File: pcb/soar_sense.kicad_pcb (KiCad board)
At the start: 4 copper layers, 42.7 x 23.1 mm, 55 parts, among them J1 Conn_02x03_Top_Bottom, J3 Conn_02x02_Top_Bottom, J4 Conn_02x02_Top_Bottom, J5 Conn_02x02_Top_Bottom, J6 Conn_02x03_Top_Bottom, J7 Conn_02x03_Top_Bottom, J8 Conn_01x06, U1 SPX3819M5-L-3-3, U2 STM32F103CBTx, U3 SHT35-DIS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

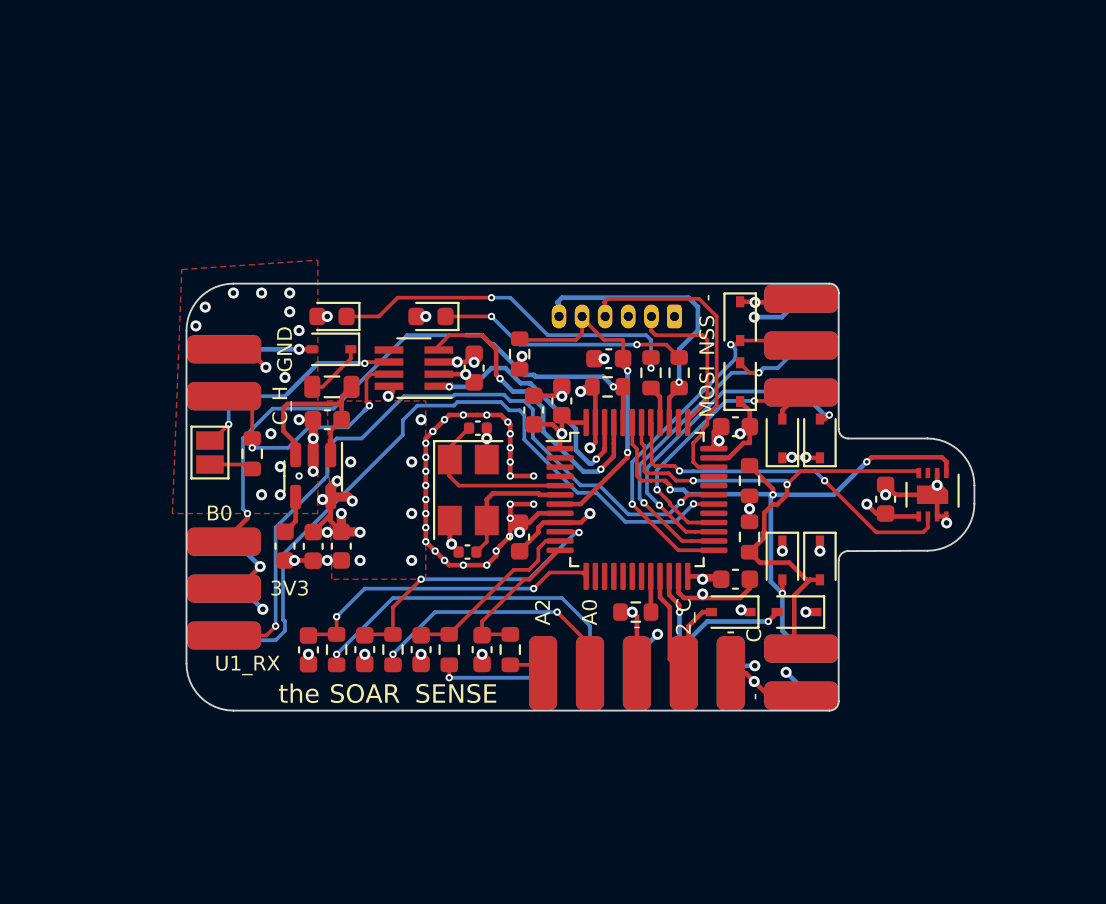
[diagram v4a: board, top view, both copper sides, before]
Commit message: added supply voltage sensing
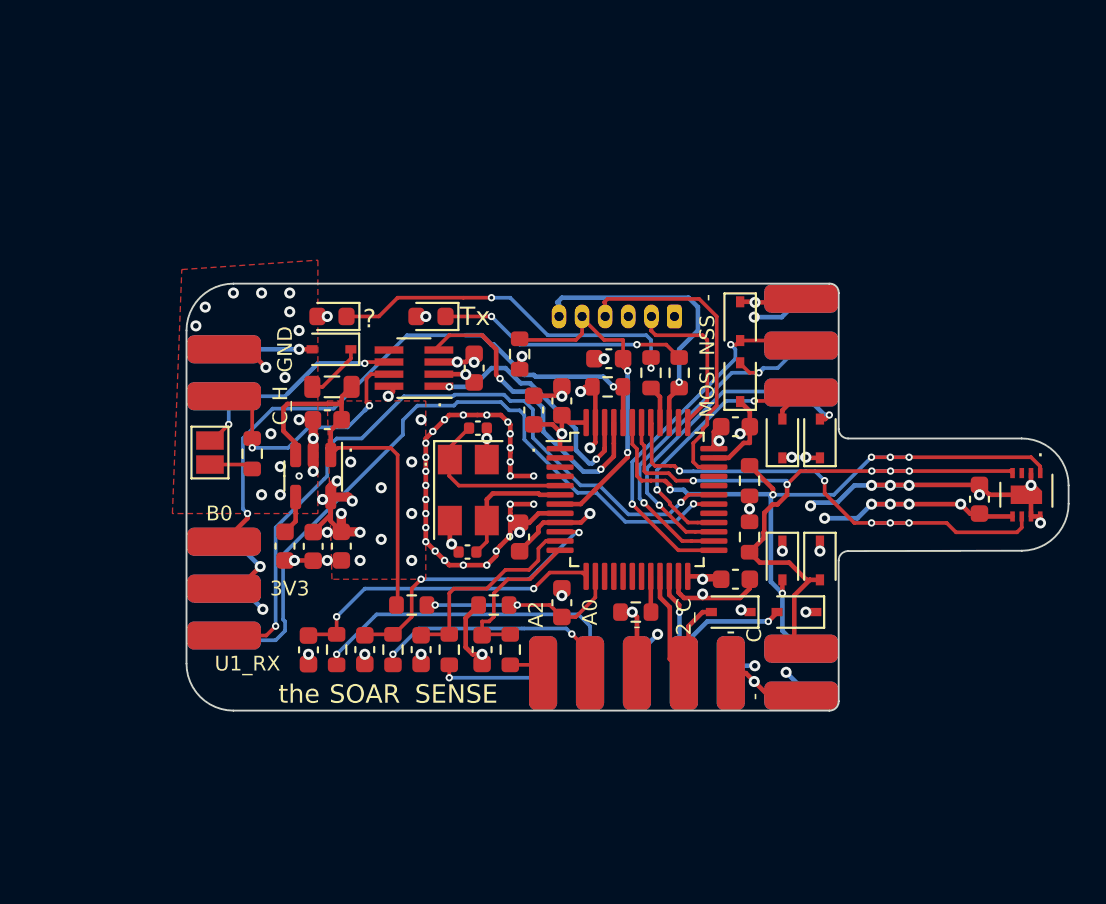
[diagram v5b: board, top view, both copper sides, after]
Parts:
- added C18: 100n, Capacitor_SMD:C_0603_1608Metric, F.Cu at (142.7, 110.7)
- added R3: 27k, Resistor_SMD:R_0603_1608Metric, F.Cu at (134.6, 110.9)
- added R4: 4k7, Resistor_SMD:R_0603_1608Metric, F.Cu at (139.1, 110.9)
- moved C13 5.08 mm to (165.4, 105.1)
- moved U3 5.08 mm to (167.9, 104.9)
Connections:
- U2 pad 14: unconnected-(U2-Pad14) -> ADC_IN4
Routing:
- net GND: track 91.5 -> 107.1 mm, vias 74 -> 79
- net Net-(C1-Pad1): track 10.3 -> 22.3 mm
- net ADC_IN4: track 0.00 -> 11.4 mm, vias 0 -> 2
- net +3V3: track 47.9 -> 57.6 mm, vias 28 -> 34
- net SHT_RST: track 19.4 -> 26.9 mm, vias 2 -> 5
- net I2C1_SCL: track 31.6 -> 38.7 mm, vias 2 -> 5
- net I2C1_SDA: track 33.8 -> 40.8 mm, vias 4 -> 6
- net ADC_IN1: track 10.0 -> 11.3 mm
- net ADC_IN2: track 8.11 -> 8.85 mm
- net ADC_INPUT3: track 18.7 -> 18.0 mm
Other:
- board size 42.7 x 23.1 mm -> 47.8 x 23.1 mm
- board text added: "."
- board text added: "12.4mm"
- board text added: "47.7mm"
- board text added: "?"
- board text added: "Tx"
- board text removed: "42.7mm"
- board text removed: "7.4mm"

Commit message: added holes
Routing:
- net GND: vias 79 -> 76
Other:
- outline, holes or cut-outs redrawn
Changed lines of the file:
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@@
     )
   )
+  (gr_line (start 127.1524 113.5888) (end 125.1204 113.5888) (layer "Edge.Cuts") (width 0.1))
   (gr_arc (start 167.64 101.854) (mid 169.436051 102.597949) (end 170.18 104.394) (layer "Edge.Cuts") (width 0.1))
   (gr_arc (start 157.734 116.078) (mid 157.588917 116.440917) (end 157.226 116.586) (layer "Edge.Cuts") (width 0.1))
+  (gr_line (start 125.1204 115.062) (end 127.1524 115.062) (layer "Edge.Cuts") (width 0.1))
+  (gr_line (start 125.222 95.9612) (end 127.254 95.9612) (layer "Edge.Cuts") (width 0.1))
   (gr_line (start 167.64 107.931949) (end 158.242 107.95) (layer "Edge.Cuts") (width 0.1))
   (gr_arc (start 122.428 96.012) (mid 123.171949 94.215949) (end 124.968 93.472) (layer "Edge.Cuts") (width 0.1))
+  (gr_arc (start 127.1524 113.5888) (mid 127.889 114.3254) (end 127.1524 115.062) (layer "Edge.Cuts") (width 0.1))
   (gr_line (start 167.64 101.854) (end 158.242 101.854) (layer "Edge.Cuts") (width 0.1))
   (gr_arc (start 170.18 105.391949) (mid 169.436051 107.188) (end 167.64 107.931949) (layer "Edge.Cuts") (width 0.1))
   (gr_arc (start 157.734 108.458) (mid 157.88279 108.09879) (end 158.242 107.95) (layer "Edge.Cuts") (width 0.1))
+  (gr_line (start 127.254 94.488) (end 125.222 94.488) (layer "Edge.Cuts") (width 0.1))
   (gr_arc (start 124.968 116.586) (mid 123.171949 115.842051) (end 122.428 114.046) (layer "Edge.Cuts") (width 0.1))
   (gr_line (start 124.968 93.472) (end 157.226 93.472) (layer "Edge.Cuts") (width 0.1))
@@
   (gr_line (start 157.734 116.078) (end 157.734 108.458) (layer "Edge.Cuts") (width 0.1))
   (gr_line (start 124.968 116.586) (end 157.226 116.586) (layer "Edge.Cuts") (width 0.1))
+  (gr_arc (start 125.222 95.9612) (mid 124.4854 95.2246) (end 125.222 94.488) (layer "Edge.Cuts") (width 0.1))
+  (gr_arc (start 127.254 94.488) (mid 127.9906 95.2246) (end 127.254 95.9612) (layer "Edge.Cuts") (width 0.1))
+  (gr_arc (start 125.1204 115.062) (mid 124.3838 114.3254) (end 125.1204 113.5888) (layer "Edge.Cuts") (width 0.1))
   (gr_line (start 120.65 93.472) (end 120.142 93.472) (layer "F.Fab") (width 0.1))
   (gr_line (start 170.18 118.618) (end 170.18 119.126) (layer "F.Fab") (width 0.1))
@@
     (effects (font (size 0.8 0.8) (thickness 0.15)))
   )
-  (gr_text "SENSE" (at 137.033 115.697) (layer "F.SilkS")
+  (gr_text "SENSE" (at 138.1252 115.7224) (layer "F.SilkS")
     (effects (font (size 1 1) (thickness 0.2)))
   )
-  (gr_text "the" (at 128.524 115.697) (layer "F.SilkS")
+  (gr_text "the" (at 129.6416 115.7224) (layer "F.SilkS")
     (effects (font (size 1 1) (thickness 0.2)))
   )
@@
     (effects (font (size 0.8 0.8) (thickness 0.15)))
   )
-  (gr_text "U1_RX" (at 125.73 114.046) (layer "F.SilkS")
+  (gr_text "U1_RX" (at 128.5748 111.4044) (layer "F.SilkS")
     (effects (font (size 0.8 0.8) (thickness 0.15)))
   )
@@
     (effects (font (size 1 1) (thickness 0.15)))
   )
-  (gr_text "SOAR" (at 132.08 115.697) (layer "F.SilkS")
+  (gr_text "SOAR" (at 133.096 115.7224) (layer "F.SilkS")
     (effects (font (size 1 1) (thickness 0.2)))
   )
@@
   (via (at 155.194 102.87) (size 0.6) (drill 0.3) (layers "F.Cu" "B.Cu") (net 2))
   (via (at 150.368 110.273503) (size 0.6) (drill 0.3) (layers "F.Cu" "B.Cu") (net 2))
-  (via (at 124.968 93.98) (size 0.6) (drill 0.3) (layers "F.Cu" "B.Cu") (net 2))
   (via (at 145.034 97.536) (size 0.6) (drill 0.3) (layers "F.Cu" "B.Cu") (net 2))
   (via (at 139.192 107.95) (size 0.4) (drill 0.2) (layers "F.Cu" "B.Cu") (net 2))
@@
   (via (at 156.21 105.5015) (size 0.6) (drill 0.3) (layers "F.Cu" "B.Cu") (net 2))
   (via (at 129.286 101.854) (size 0.6) (drill 0.3) (layers "F.Cu" "B.Cu") (net 2))
-  (via (at 122.936 95.758) (size 0.6) (drill 0.3) (layers "F.Cu" "B.Cu") (net 2))
-  (via (at 123.444 94.742) (size 0.6) (drill 0.3) (layers "F.Cu" "B.Cu") (net 2))
   (via (at 139.954 102.362) (size 0.4) (drill 0.2) (layers "F.Cu" "B.Cu") (net 2))
   (via (at 146.558 111.252) (size 0.6) (drill 0.3) (layers "F.Cu" "B.Cu") (net 2))
@@
   (via (at 136.779 107.569) (size 0.6) (drill 0.3) (layers "F.Cu" "B.Cu") (net 2))
   (via (at 154.686 107.95) (size 0.6) (drill 0.3) (layers "F.Cu" "B.Cu") (net 2))
-  (via (at 126.492 93.98) (size 0.6) (drill 0.3) (layers "F.Cu" "B.Cu") (net 2))
   (via (at 127 101.6) (size 0.6) (drill 0.3) (layers "F.Cu" "B.Cu") (net 2))
+  (via (at 123.0884 95.758) (size 0.6) (drill 0.3) (layers "F.Cu" "B.Cu") (net 2))
   (via (at 168.656 106.426) (size 0.6) (drill 0.3) (layers "F.Cu" "B.Cu") (net 2))
   (via (at 126.492 104.902) (size 0.6) (drill 0.3) (layers "F.Cu" "B.Cu") (net 2))
@@
   (via (at 136.398 108.458) (size 0.4) (drill 0.2) (layers "F.Cu" "B.Cu") (net 2))
   (via (at 138.684 100.584) (size 0.4) (drill 0.2) (layers "F.Cu" "B.Cu") (net 2))
+  (via (at 124.2568 94.1832) (size 0.6) (drill 0.3) (layers "F.Cu" "B.Cu") (net 2))
   (via (at 141.224 103.886) (size 0.4) (drill 0.2) (layers "F.Cu" "B.Cu") (net 2))
   (via (at 138.43 113.538) (size 0.6) (drill 0.3) (layers "F.Cu" "B.Cu") (net 2))
@@
   (via (at 130.048 108.458) (size 0.6) (drill 0.3) (layers "F.Cu" "B.Cu") (net 2))
   (via (at 128.524 103.886) (size 0.4) (drill 0.2) (layers "F.Cu" "B.Cu") (free) (net 2))
-  (via (at 128.016 94.996) (size 0.6) (drill 0.3) (layers "F.Cu" "B.Cu") (net 2))
   (via (at 155.956 102.87) (size 0.6) (drill 0.3) (layers "F.Cu" "B.Cu") (net 2))
   (via (at 161.544 104.394) (size 0.6) (drill 0.3) (layers "F.Cu" "B.Cu") (net 2))
